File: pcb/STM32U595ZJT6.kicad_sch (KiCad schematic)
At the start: 43 parts, among them J3 Conn_ST_STDC14, J4 Conn_ST_STDC14, U7 STM32U595ZJTx, Y2 16MHz, Y4 16MHz

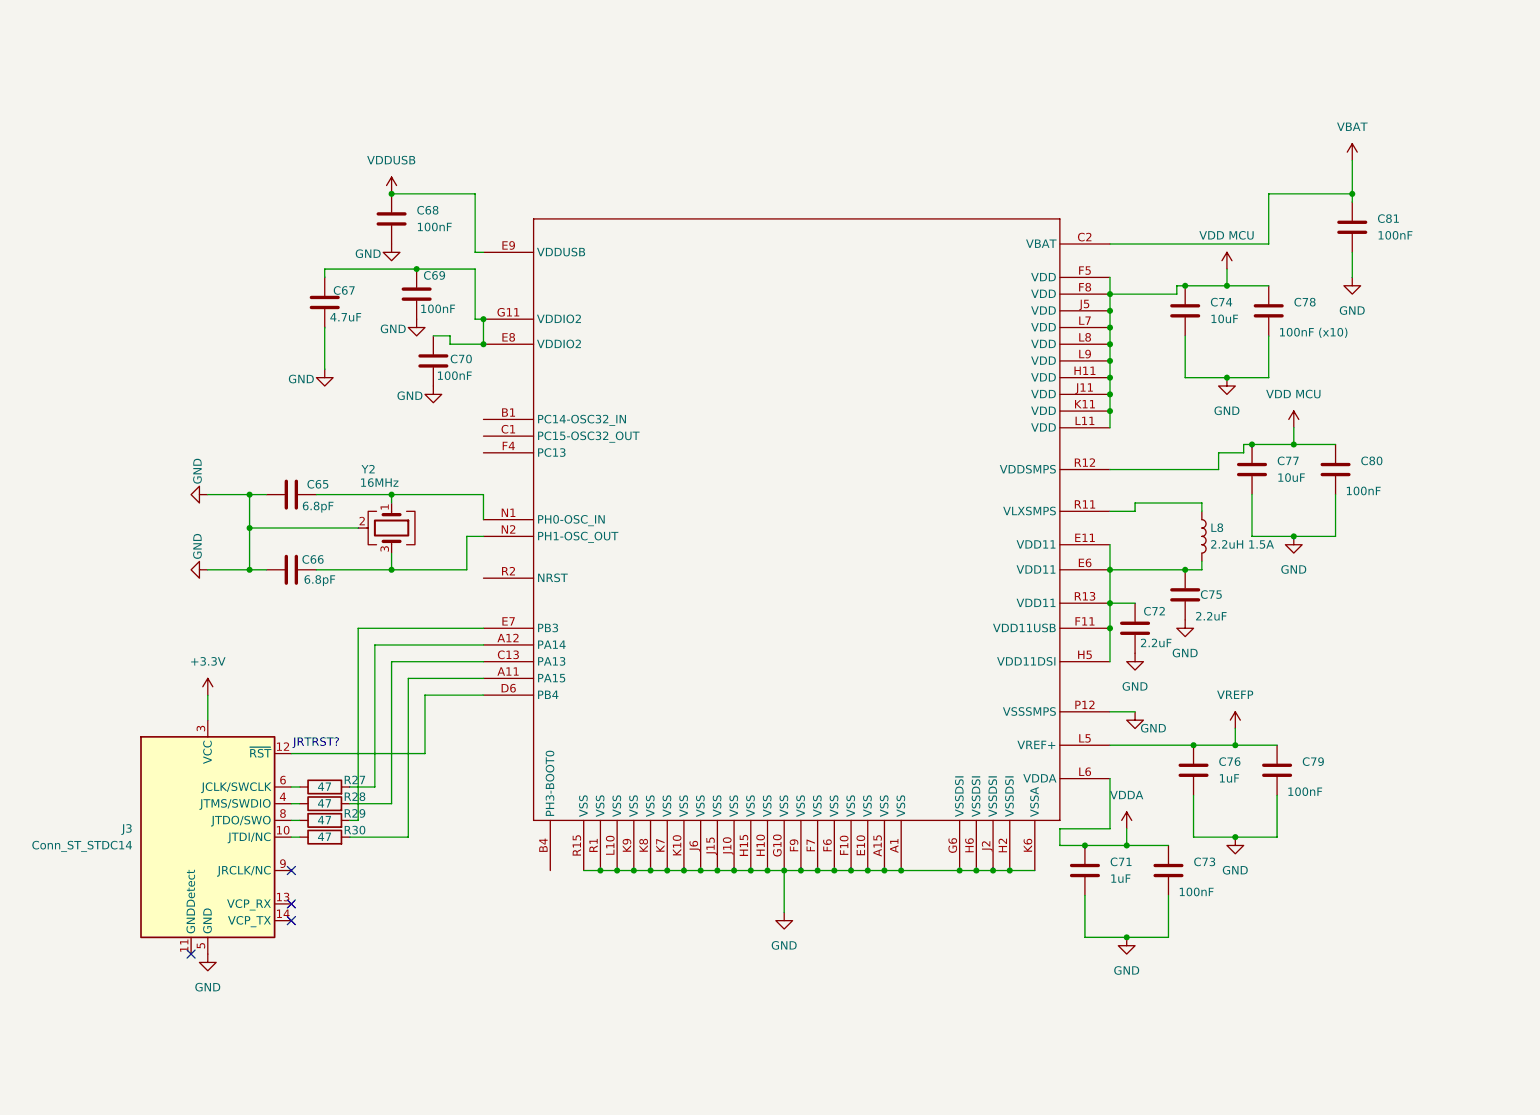
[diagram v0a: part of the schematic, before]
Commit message: initial new mcu design complete
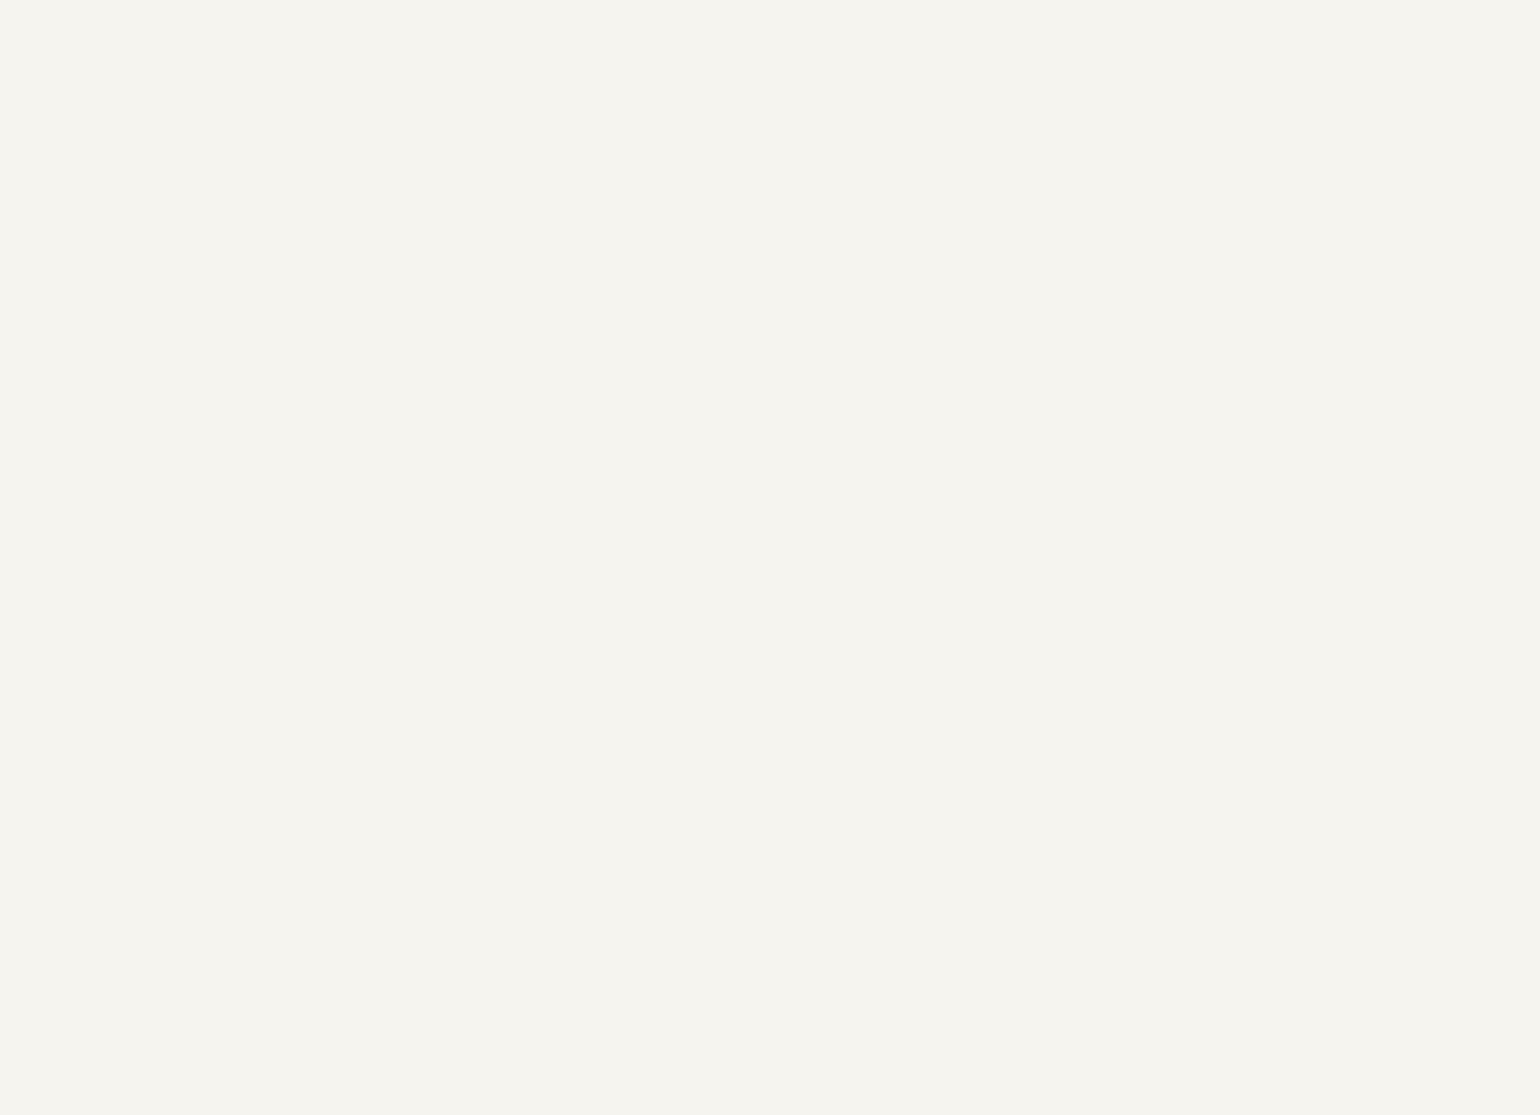
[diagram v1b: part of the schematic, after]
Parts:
- removed C65, C66: 6.8pF, symbol Device:C
- removed C67: 4.7uF, symbol Device:C
- removed C68, C69, C70, C73, C79, C80, C81: 100nF, symbol Device:C
- removed C71, C76: 1uF, symbol Device:C
- removed C72, C75: 2.2uF, symbol Device:C
- removed C74, C77: 10uF, symbol Device:C
- removed C78: 100nF (x10), symbol Device:C
- removed J3: Conn_ST_STDC14, symbol Connector:Conn_ST_STDC14
- removed L8: 2.2uH 1.5A, Package_SON:WSON-8-1EP_6x5mm_P1.27mm_EP3.4x4mm, symbol Device:L
- removed R27, R28, R29, R30: 47, symbol Device:R
- removed STM32UF9NJH6Q_CUSTOM2: (no value), symbol STM32U5F0NJH6Q_custom:STM32U5F9NJH6Q_CUSTOM
- removed Y2: 16MHz, Oscillator:Oscillator_SMD_Fordahl_DFAS11-4Pin_7.0x5.0mm, symbol Device:Crystal_GND24
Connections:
- no-connect marks 8 -> 4
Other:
- note removed: "JRTRST?"

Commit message: fixed decoupling capacitors
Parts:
- removed C83: 10uF, symbol Device:C
- removed C84: 100nF (x5), symbol Device:C
- added C100, C101, C102, C94, C95, C96, C97, C98, C99: 100nF, symbol Device:C
- added C93: 10uF, symbol Device:C
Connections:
- net +3.3V: now also U7.108 (VDD), U7.121 (VDD), U7.144 (VDD), U7.17 (VDD), U7.39 (VDD), U7.52 (VDD), U7.62 (VDD), U7.72 (VDD), U7.84 (VDD), C100.1, C101.1, C102.1, C93.1, C94.1, C95.1, C96.1, C97.1, C98.1, C99.1
- net GND: now also C100.2, C101.2, C102.2, C93.2, C94.2, C95.2, C96.2, C97.2, C98.2, C99.2
- net VDDUSB: no longer U7.108 (VDD), U7.121 (VDD), U7.144 (VDD), U7.17 (VDD), U7.39 (VDD), U7.52 (VDD), U7.62 (VDD), U7.72 (VDD), U7.84 (VDD)
